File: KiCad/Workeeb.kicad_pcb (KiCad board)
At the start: 2 copper layers, 224 parts, among them J1 USB_C_Receptacle_USB2.0, U1 EFM32HG322F64G-C-QFP48

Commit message: Connect up row diodes
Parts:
- moved C_DEC1 118.9 mm to (468.0, 28.1)
- moved C_IOVDD_3 118.9 mm to (468.0, 31.1)
- moved C_VDD_1 118.9 mm to (465.8, 34.1)
- moved C_VREGI1 118.9 mm to (451.5, 23.6)
- moved C_AVDD1 118.9 mm to (463.6, 29.6)
- moved C_AVDD_0 118.9 mm to (463.6, 26.6)
- moved C_DEC2 118.9 mm to (474.7, 32.7)
- moved C_IOVDD1 118.9 mm to (460.4, 23.6)
- moved C_IOVDD_5 118.9 mm to (470.2, 37.1)
- moved C_RESET1 118.9 mm to (470.2, 34.1)
- moved C_VDD1 118.9 mm to (474.7, 35.7)
- moved C_VREGO1 118.9 mm to (456.0, 23.6)
- moved FB_VBUS1 118.9 mm to (465.6, 18.6)
- moved R_CC1 118.9 mm to (454.7, 29.5)
- moved R_CC2 118.9 mm to (454.7, 26.6)
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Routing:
- net ROW2: track 0.00 -> 380.6 mm
- net ROW6: track 0.00 -> 372.6 mm
- net ROW5: track 0.00 -> 354.6 mm
- net ROW4: track 0.00 -> 347.2 mm
- net ROW3: track 47.5 -> 352.1 mm
- net Net-(D100-Pad2): track 0.00 -> 22.0 mm
- net Net-(D69-Pad2): track 0.00 -> 19.0 mm
- net Net-(D7-Pad2): track 0.00 -> 19.0 mm
- net ROW1: track 295.2 -> 313.9 mm
- net Net-(D73-Pad2): track 0.00 -> 16.5 mm
- net Net-(D92-Pad2): track 0.00 -> 15.8 mm
- net Net-(D70-Pad2): track 0.00 -> 14.2 mm
- net Net-(D4-Pad2): track 0.00 -> 14.2 mm
- net Net-(D3-Pad2): track 0.00 -> 11.0 mm
- net Net-(D5-Pad2): track 0.00 -> 9.46 mm
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
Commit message: Route all left-side cols to MCU area
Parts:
- turned U1 to -90 degrees
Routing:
- net COL1: track 0.00 -> 457.3 mm, vias 0 -> 1
- net COL4: track 0.00 -> 409.2 mm, vias 0 -> 1
- net COL3: track 0.00 -> 403.0 mm, vias 0 -> 1
- net COL2: track 0.00 -> 387.6 mm, vias 0 -> 1
- net COL5: track 0.00 -> 367.7 mm, vias 0 -> 1
- net COL6: track 0.00 -> 347.2 mm, vias 0 -> 1
- net COL7: track 0.00 -> 333.9 mm, vias 0 -> 1
- net COL8: track 0.00 -> 317.1 mm, vias 0 -> 1
- net COL9: track 0.00 -> 297.3 mm, vias 0 -> 1
- net COL11: track 0.00 -> 291.7 mm, vias 0 -> 1
- net COL10: track 0.00 -> 278.9 mm, vias 0 -> 1
- net COL12: track 0.00 -> 252.8 mm, vias 0 -> 1
- net COL13: track 0.00 -> 233.6 mm, vias 0 -> 1
- net COL14: track 0.00 -> 227.2 mm, vias 0 -> 1
- net COL15: track 0.00 -> 199.2 mm, vias 0 -> 1
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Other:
- board text added: "25 mils for via placement"
- board text added: "31.25 mils for Diode placement"

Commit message: Reorder row/cols to match physical layout of routes better
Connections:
- U1 pad 11: COL2 -> ROW1
- U1 pad 12: COL3 -> ROW2
- U1 pad 13: COL4 -> ROW3
- U1 pad 14: unconnected-(U1-Pad14) -> ROW4
- U1 pad 15: unconnected-(U1-Pad15) -> ROW5
- U1 pad 17: unconnected-(U1-Pad17) -> ROW6
- U1 pad 2: ROW1 -> COL7
- U1 pad 25: COL5 -> BADGE
- U1 pad 26: COL6 -> NUMLK
- U1 pad 27: COL7 -> CAPS
- U1 pad 3: ROW2 -> COL6
- U1 pad 30: COL8 -> COL20
- U1 pad 31: COL9 -> COL19
- U1 pad 32: COL10 -> COL18
- U1 pad 37: COL11 -> COL17
- U1 pad 38: COL12 -> COL16
- U1 pad 39: COL13 -> COL15
- U1 pad 41: COL15 -> COL13
- U1 pad 42: COL16 -> COL12
- U1 pad 45: COL17 -> COL11
- U1 pad 46: COL18 -> COL10
- U1 pad 47: COL19 -> COL9
- U1 pad 48: COL20 -> COL8
- U1 pad 6: ROW3 -> COL5
- U1 pad 7: ROW4 -> COL4
- U1 pad 8: ROW5 -> COL3
- U1 pad 9: ROW6 -> COL2
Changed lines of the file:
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@@
   (net 131 "COL20")
   (net 132 "Net-(C_DEC1-Pad1)")
-  (net 133 "unconnected-(U1-Pad14)")
-  (net 134 "unconnected-(U1-Pad15)")
+  (net 133 "BADGE")
+  (net 134 "NUMLK")
   (net 135 "RESET")
-  (net 136 "unconnected-(U1-Pad17)")
+  (net 136 "CAPS")
   (net 137 "VBUS")
   (net 138 "Net-(FB_VBUS1-Pad1)")
@@
       (net 150 "DMPU") (pinfunction "PA0") (pintype "bidirectional"))
     (pad "2" smd rect locked (at -4.1148 2.250001 180) (size 0.254 1.461999) (layers "B.Cu" "B.Paste" "B.Mask")
-      (net 1 "ROW1") (pinfunction "PA1") (pintype "bidirectional"))
+      (net 19 "COL7") (pinfunction "PA1") (pintype "bidirectional"))
     (pad "3" smd rect locked (at -4.1148 1.749999 180) (size 0.254 1.461999) (layers "B.Cu" "B.Paste" "B.Mask")
-      (net 2 "ROW2") (pinfunction "PA2") (pintype "bidirectional"))
+      (net 17 "COL6") (pinfunction "PA2") (pintype "bidirectional"))
     (pad "4" smd rect locked (at -4.1148 1.25 180) (size 0.254 1.461999) (layers "B.Cu" "B.Paste" "B.Mask")
       (net 126 "VDD") (pinfunction "IOVDD_0") (pintype "power_in"))
@@
       (net 127 "GND") (pinfunction "VSS") (pintype "power_in"))
     (pad "6" smd rect locked (at -4.1148 0.25 180) (size 0.254 1.461999) (layers "B.Cu" "B.Paste" "B.Mask")
-      (net 4 "ROW3") (pinfunction "PC0") (pintype "bidirectional"))
+      (net 16 "COL5") (pinfunction "PC0") (pintype "bidirectional"))
     (pad "7" smd rect locked (at -4.1148 -0.25 180) (size 0.254 1.461999) (layers "B.Cu" "B.Paste" "B.Mask")
-      (net 6 "ROW4") (pinfunction "PC1") (pintype "bidirectional"))
+      (net 15 "COL4") (pinfunction "PC1") (pintype "bidirectional"))
     (pad "8" smd rect locked (at -4.1148 -0.750001 180) (size 0.254 1.461999) (layers "B.Cu" "B.Paste" "B.Mask")
-      (net 9 "ROW5") (pinfunction "PC2") (pintype "bidirectional"))
+      (net 13 "COL3") (pinfunction "PC2") (pintype "bidirectional"))
     (pad "9" smd rect locked (at -4.1148 -1.25 180) (size 0.254 1.461999) (layers "B.Cu" "B.Paste" "B.Mask")
-      (net 8 "ROW6") (pinfunction "PC3") (pintype "bidirectional"))
+      (net 12 "COL2") (pinfunction "PC3") (pintype "bidirectional"))
     (pad "10" smd rect locked (at -4.1148 -1.749999 180) (size 0.254 1.461999) (layers "B.Cu" "B.Paste" "B.Mask")
       (net 11 "COL1") (pinfunction "PC4") (pintype "bidirectional"))
     (pad "11" smd rect locked (at -4.1148 -2.250001 180) (size 0.254 1.461999) (layers "B.Cu" "B.Paste" "B.Mask")
-      (net 12 "COL2") (pinfunction "PB7") (pintype "bidirectional"))
+      (net 1 "ROW1") (pinfunction "PB7") (pintype "bidirectional"))
     (pad "12" smd rect locked (at -4.1148 -2.75 180) (size 0.254 1.461999) (layers "B.Cu" "B.Paste" "B.Mask")
-      (net 13 "COL3") (pinfunction "PB8") (pintype "bidirectional"))
+      (net 2 "ROW2") (pinfunction "PB8") (pintype "bidirectional"))
     (pad "13" smd rect locked (at -2.75 -4.1148 270) (size 0.254 1.461999) (layers "B.Cu" "B.Paste" "B.Mask")
-      (net 15 "COL4") (pinfunction "PA8") (pintype "bidirectional"))
+      (net 4 "ROW3") (pinfunction "PA8") (pintype "bidirectional"))
     (pad "14" smd rect locked (at -2.250001 -4.1148 270) (size 0.254 1.461999) (layers "B.Cu" "B.Paste" "B.Mask")
-      (net 133 "unconnected-(U1-Pad14)") (pinfunction "PA9") (pintype "bidirectional+no_connect"))
+      (net 6 "ROW4") (pinfunction "PA9") (pintype "bidirectional"))
     (pad "15" smd rect locked (at -1.749999 -4.1148 270) (size 0.254 1.461999) (layers "B.Cu" "B.Paste" "B.Mask")
-      (net 134 "unconnected-(U1-Pad15)") (pinfunction "PA10") (pintype "bidirectional+no_connect"))
+      (net 9 "ROW5") (pinfunction "PA10") (pintype "bidirectional"))
     (pad "16" smd rect locked (at -1.25 -4.1148 270) (size 0.254 1.461999) (layers "B.Cu" "B.Paste" "B.Mask")
       (net 135 "RESET") (pinfunction "RESETn") (pintype "unspecified"))
     (pad "17" smd rect locked (at -0.750001 -4.1148 270) (size 0.254 1.461999) (layers "B.Cu" "B.Paste" "B.Mask")
-      (net 136 "unconnected-(U1-Pad17)") (pinfunction "PB11") (pintype "bidirectional+no_connect"))
+      (net 8 "ROW6") (pinfunction "PB11") (pintype "bidirectional"))
     (pad "18" smd rect locked (at -0.25 -4.1148 270) (size 0.254 1.461999) (layers "B.Cu" "B.Paste" "B.Mask")
       (net 127 "GND") (pinfunction "VSS") (pintype "power_in"))
@@
       (net 143 "unconnected-(U1-Pad24)") (pinfunction "PD4") (pintype "bidirectional+no_connect"))
     (pad "25" smd rect locked (at 4.1148 -2.75 180) (size 0.254 1.461999) (layers "B.Cu" "B.Paste" "B.Mask")
-      (net 16 "COL5") (pinfunction "PD5") (pintype "bidirectional"))
+      (net 133 "BADGE") (pinfunction "PD5") (pintype "bidirectional"))
     (pad "26" smd rect locked (at 4.1148 -2.250001 180) (size 0.254 1.461999) (layers "B.Cu" "B.Paste" "B.Mask")
-      (net 17 "COL6") (pinfunction "PD6") (pintype "bidirectional"))
+      (net 134 "NUMLK") (pinfunction "PD6") (pintype "bidirectional"))
     (pad "27" smd rect locked (at 4.1148 -1.749999 180) (size 0.254 1.461999) (layers "B.Cu" "B.Paste" "B.Mask")
-      (net 19 "COL7") (pinfunction "PD7") (pintype "bidirectional"))
+      (net 136 "CAPS") (pinfunction "PD7") (pintype "bidirectional"))
     (pad "28" smd rect locked (at 4.1148 -1.25 180) (size 0.254 1.461999) (layers "B.Cu" "B.Paste" "B.Mask")
       (net 126 "VDD") (pinfunction "VDD_DREG") (pintype "power_in"))
@@
       (net 132 "Net-(C_DEC1-Pad1)") (pinfunction "DECOUPLE") (pintype "unspecified"))
     (pad "30" smd rect locked (at 4.1148 -0.25 180) (size 0.254 1.461999) (layers "B.Cu" "B.Paste" "B.Mask")
-      (net 20 "COL8") (pinfunction "PC8") (pintype "bidirectional"))
+      (net 131 "COL20") (pinfunction "PC8") (pintype "bidirectional"))
     (pad "31" smd rect locked (at 4.1148 0.25 180) (size 0.254 1.461999) (layers "B.Cu" "B.Paste" "B.Mask")
-      (net 21 "COL9") (pinfunction "PC9") (pintype "bidirectional"))
+      (net 130 "COL19") (pinfunction "PC9") (pintype "bidirectional"))
     (pad "32" smd rect locked (at 4.1148 0.750001 180) (size 0.254 1.461999) (layers "B.Cu" "B.Paste" "B.Mask")
-      (net 26 "COL10") (pinfunction "PC10") (pintype "bidirectional"))
+      (net 129 "COL18") (pinfunction "PC10") (pintype "bidirectional"))
     (pad "33" smd rect locked (at 4.1148 1.25 180) (size 0.254 1.461999) (layers "B.Cu" "B.Paste" "B.Mask")
       (net 137 "VBUS") (pinfunction "USB_VREGI") (pintype "unspecified"))
@@
       (net 148 "D+") (pinfunction "PC15") (pintype "bidirectional"))
     (pad "37" smd rect locked (at 2.75 4.1148 270) (size 0.254 1.461999) (layers "B.Cu" "B.Paste" "B.Mask")
-      (net 29 "COL11") (pinfunction "PF0") (pintype "bidirectional"))
+      (net 128 "COL17") (pinfunction "PF0") (pintype "bidirectional"))
     (pad "38" smd rect locked (at 2.250001 4.1148 270) (size 0.254 1.461999) (layers "B.Cu" "B.Paste" "B.Mask")
-      (net 33 "COL12") (pinfunction "PF1") (pintype "bidirectional"))
+      (net 125 "COL16") (pinfunction "PF1") (pintype "bidirectional"))
     (pad "39" smd rect locked (at 1.749999 4.1148 270) (size 0.254 1.461999) (layers "B.Cu" "B.Paste" "B.Mask")
-      (net 37 "COL13") (pinfunction "PF2") (pintype "bidirectional"))
+      (net 124 "COL15") (pinfunction "PF2") (pintype "bidirectional"))
     (pad "40" smd rect locked (at 1.25 4.1148 270) (size 0.254 1.461999) (layers "B.Cu" "B.Paste" "B.Mask")
       (net 123 "COL14") (pinfunction "PF3") (pintype "bidirectional"))
     (pad "41" smd rect locked (at 0.750001 4.1148 270) (size 0.254 1.461999) (layers "B.Cu" "B.Paste" "B.Mask")
-      (net 124 "COL15") (pinfunction "PF4") (pintype "bidirectional"))
+      (net 37 "COL13") (pinfunction "PF4") (pintype "bidirectional"))
     (pad "42" smd rect locked (at 0.25 4.1148 270) (size 0.254 1.461999) (layers "B.Cu" "B.Paste" "B.Mask")
-      (net 125 "COL16") (pinfunction "PF5") (pintype "bidirectional"))
+      (net 33 "COL12") (pinfunction "PF5") (pintype "bidirectional"))
     (pad "43" smd rect locked (at -0.25 4.1148 270) (size 0.254 1.461999) (layers "B.Cu" "B.Paste" "B.Mask")
       (net 126 "VDD") (pinfunction "IOVDD_5") (pintype "power_in"))
@@
       (net 127 "GND") (pinfunction "VSS") (pintype "power_in"))
     (pad "45" smd rect locked (at -1.25 4.1148 270) (size 0.254 1.461999) (layers "B.Cu" "B.Paste" "B.Mask")
-      (net 128 "COL17") (pinfunction "PE10") (pintype "bidirectional"))
+      (net 29 "COL11") (pinfunction "PE10") (pintype "bidirectional"))
     (pad "46" smd rect locked (at -1.749999 4.1148 270) (size 0.254 1.461999) (layers "B.Cu" "B.Paste" "B.Mask")
-      (net 129 "COL18") (pinfunction "PE11") (pintype "bidirectional"))
+      (net 26 "COL10") (pinfunction "PE11") (pintype "bidirectional"))
     (pad "47" smd rect locked (at -2.250001 4.1148 270) (size 0.254 1.461999) (layers "B.Cu" "B.Paste" "B.Mask")
-      (net 130 "COL19") (pinfunction "PE12") (pintype "bidirectional"))
+      (net 21 "COL9") (pinfunction "PE12") (pintype "bidirectional"))
     (pad "48" smd rect locked (at -2.75 4.1148 270) (size 0.254 1.461999) (layers "B.Cu" "B.Paste" "B.Mask")
-      (net 131 "COL20") (pinfunction "PE13") (pintype "bidirectional"))
+      (net 20 "COL8") (pinfunction "PE13") (pintype "bidirectional"))
   )
   (footprint "Diode_SMD:D_SOD-123" (layer "B.Cu")

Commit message: Moved diodes into new place for better col routing
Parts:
- moved D100 16.2 mm to (426.2, 94.5)
- moved D97 10.7 mm to (406.4, 142.1), turned to 90 degrees
- moved D95 10.7 mm to (406.4, 104.0), turned to 90 degrees
- moved D19 10.7 mm to (97.6, 142.1), turned to 90 degrees
- moved D34 10.7 mm to (167.5, 142.1), turned to 90 degrees
- moved D5 10.7 mm to (50.0, 142.1), turned to 90 degrees
- moved D55 10.7 mm to (235.7, 142.1), turned to 90 degrees
- moved D61 10.7 mm to (254.8, 142.1), turned to 90 degrees
- moved D66 10.7 mm to (273.8, 142.1), turned to 90 degrees
- moved D8 10.7 mm to (73.8, 142.1), turned to 90 degrees
- moved D92 10.7 mm to (388.1, 142.1), turned to 90 degrees
- moved D11 10.7 mm to (73.8, 84.9), turned to 90 degrees
- moved D16 10.7 mm to (92.9, 84.9), turned to 90 degrees
- moved D22 10.7 mm to (111.9, 84.9), turned to 90 degrees
- moved D27 10.7 mm to (131.0, 84.9), turned to 90 degrees
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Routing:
- net ROW3: track 352.1 -> 396.0 mm
- net ROW5: track 354.6 -> 391.2 mm
- net ROW6: track 372.6 -> 360.3 mm
- net Net-(D100-Pad2): track 22.0 -> 10.3 mm
- net Net-(D12-Pad2): track 6.29 -> 10.3 mm
- net Net-(D89-Pad2): track 6.29 -> 10.3 mm
- net Net-(D85-Pad2): track 6.29 -> 10.3 mm
- net Net-(D79-Pad2): track 6.29 -> 10.3 mm
- net Net-(D39-Pad2): track 6.29 -> 10.3 mm
- net Net-(D29-Pad2): track 6.29 -> 10.3 mm
- net Net-(D3-Pad2): track 11.0 -> 14.8 mm
- net Net-(D92-Pad2): track 15.8 -> 19.6 mm
- net Net-(D93-Pad2): track 6.93 -> 10.3 mm
- net Net-(D88-Pad2): track 6.93 -> 10.3 mm
- net Net-(D78-Pad2): track 6.93 -> 10.3 mm
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
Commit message: Removed old vias
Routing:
- net COL15: track 199.2 -> 213.4 mm, vias 1 -> 0
- net COL17: track 84.2 -> 93.7 mm, vias 1 -> 0
- net COL9: track 297.3 -> 291.8 mm, vias 1 -> 0
- net COL11: track 291.7 -> 286.3 mm, vias 1 -> 0
- net COL10: track 278.9 -> 273.5 mm, vias 1 -> 0
- net COL8: track 317.1 -> 311.7 mm, vias 1 -> 0
- net COL7: track 333.9 -> 329.5 mm, vias 1 -> 0
- net COL2: track 387.6 -> 383.2 mm, vias 1 -> 0
- net COL13: track 233.6 -> 237.7 mm, vias 1 -> 0
- net COL12: track 252.8 -> 257.0 mm, vias 1 -> 0
- net COL3: track 403.0 -> 406.7 mm, vias 1 -> 0
- net COL1: track 457.3 -> 460.4 mm, vias 1 -> 0
- net COL6: track 347.2 -> 350.2 mm, vias 1 -> 0
- net COL5: track 367.7 -> 370.8 mm, vias 1 -> 0
- net COL16: track 151.8 -> 154.8 mm, vias 1 -> 0
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
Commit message: Start to do power routing
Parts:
- removed C_AVDD_0: 10nF, Capacitor_SMD:C_0805_2012Metric
- removed C_IOVDD_0, C_IOVDD_5: 0.1uF, Capacitor_SMD:C_0805_2012Metric
- added C_AVDD_2: 10nF, Capacitor_SMD:C_0805_2012Metric, F.Cu at (468.8, -5.03)
- added C_IOVDD_1: 0.1uF, Capacitor_SMD:C_0805_2012Metric, F.Cu at (466.8, -8.04)
- added C_IOVDD_2: 0.1uF, Capacitor_SMD:C_0805_2012Metric, F.Cu at (453.2, -3.17)
- added D101: SK6812, LED_SMD:LED_SK6812_PLCC4_5.0x5.0mm_P3.2mm, F.Cu at (416.7, 33.3)
- added D102: LED, LED_SMD:LED_1206_3216Metric_Pad1.42x1.75mm_HandSolder, F.Cu at (378.6, 33.3)
- added D103: LED, LED_SMD:LED_1206_3216Metric_Pad1.42x1.75mm_HandSolder, F.Cu at (397.7, 33.3)
- MX83: value Knob -> Num Lock; footprint Rotary_Encoder:RotaryEncoder_Alps_EC12E-Switch_Vertical_H20mm -> MX_Only:MXOnly-1U-NoLED
- MX84: value Num Lock -> num7
- MX85: value num7 -> num4
- MX86: value num4 -> num1
- MX87: value num1 -> Knob; footprint MX_Only:MXOnly-1U-NoLED -> Rotary_Encoder:RotaryEncoder_Alps_EC12E-Switch_Vertical_H20mm
- moved MX87 93.0 mm to (362.1, 26.1), turned to -90 degrees
- moved MX83 35.8 mm to (359.6, 61.9), turned to 0 degrees
- moved MX84 19.1 mm to (359.6, 81.0)
- moved MX85 19.0 mm to (359.6, 100.0)
- moved MX86 19.0 mm to (359.6, 119.1)
- moved C_VREGI1 13.2 mm to (442.1, 14.3)
- moved U1 4.48 mm to (386.6, 45.2)
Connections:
- MX84 pad 2: Net-(D84-Pad2) -> Net-(D85-Pad2)
- MX85 pad 2: Net-(D85-Pad2) -> Net-(D86-Pad2)
- MX86 pad 2: Net-(D86-Pad2) -> Net-(D87-Pad2)
- R_CC1 pad 1: Net-(J1-PadA5) -> Net-(J1-PadB5)
- R_CC2 pad 1: Net-(J1-PadB5) -> Net-(J1-PadA5)
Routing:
- net VDD: track 0.00 -> 11.5 mm, vias 0 -> 6

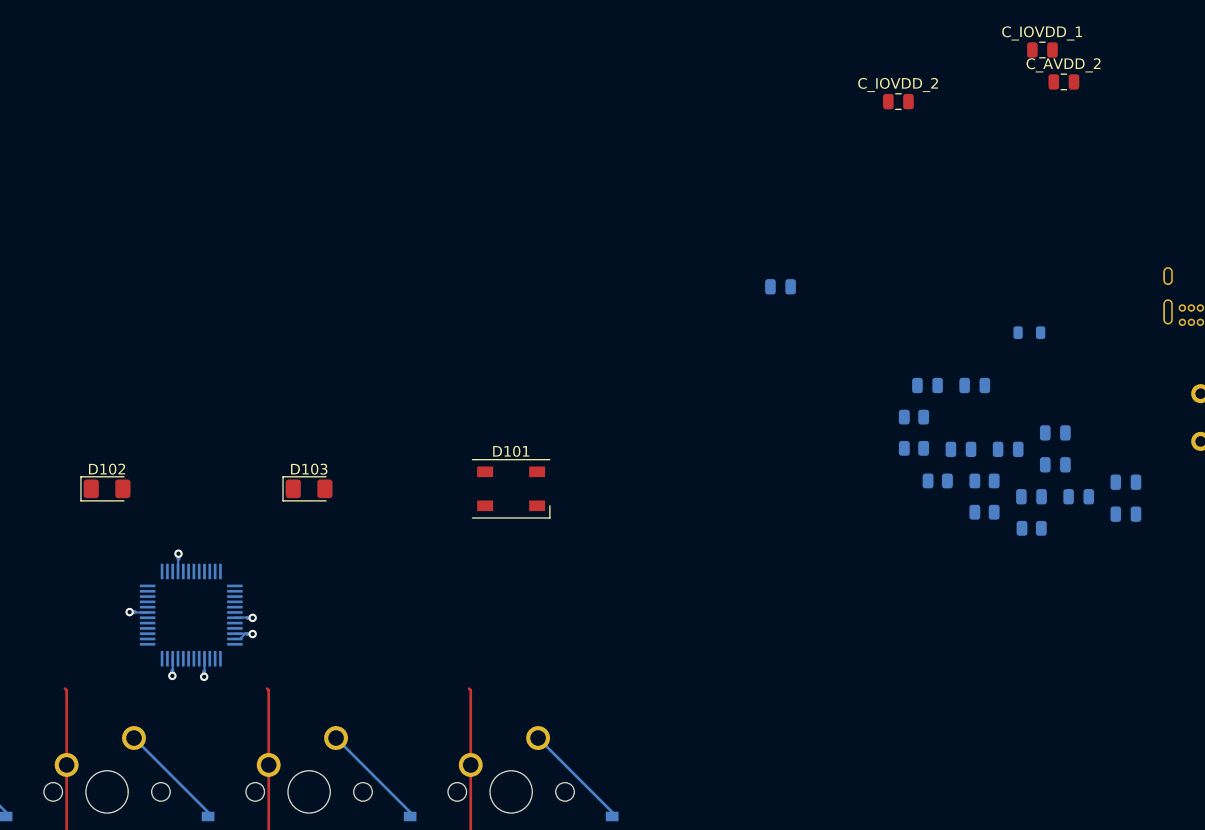
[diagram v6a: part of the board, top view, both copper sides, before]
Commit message: Better cap names, start placing decoupling caps
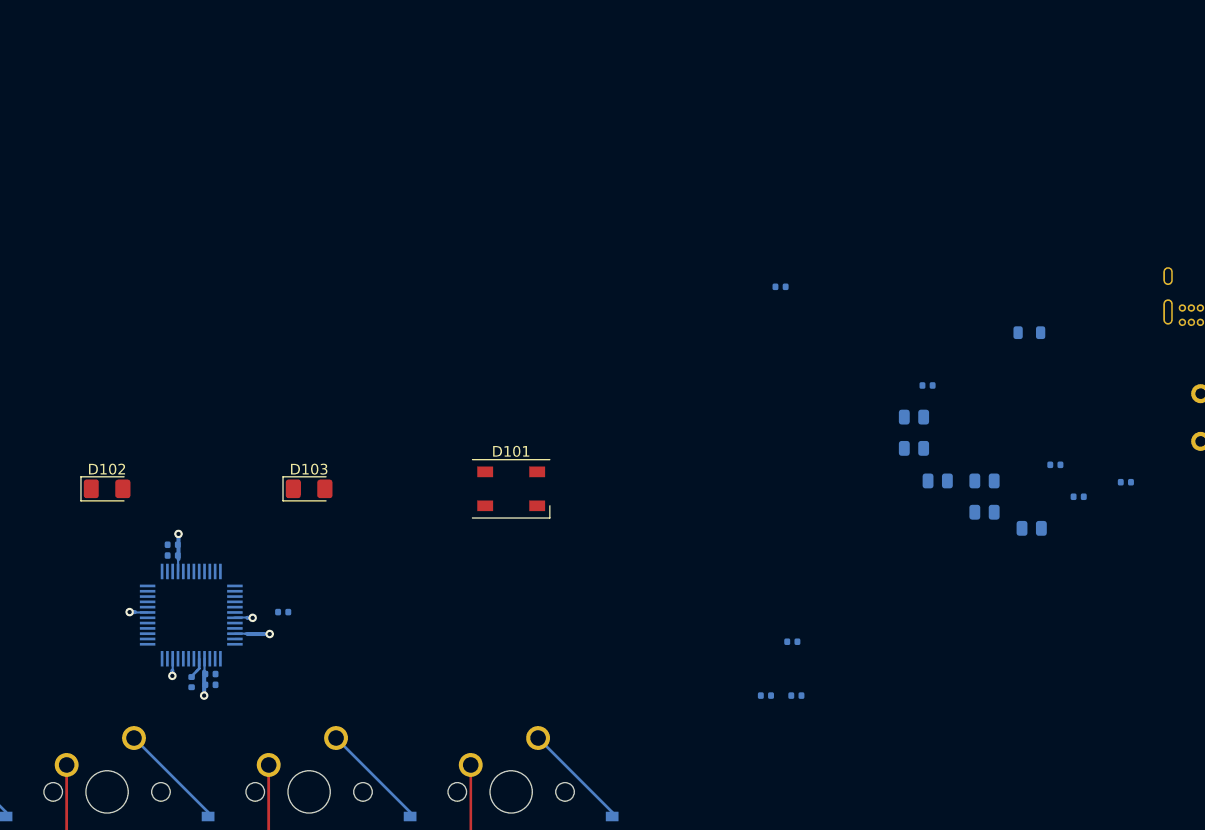
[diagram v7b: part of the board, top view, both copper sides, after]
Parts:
- removed C_AVDD1, C_IOVDD1, C_VDD1: 10uF, Capacitor_SMD:C_0805_2012Metric
- removed C_AVDD_2: 10nF, Capacitor_SMD:C_0805_2012Metric
- removed C_IOVDD_1, C_IOVDD_2, C_VDD_1: 0.1uF, Capacitor_SMD:C_0805_2012Metric
- added C_AVDD0: 10uF, Capacitor_SMD:C_0402_1005Metric, B.Cu at (440.7, 52.8)
- added C_AVDD_0: 10nF, Capacitor_SMD:C_0402_1005Metric, B.Cu at (443.6, 52.8)
- added C_DREG1: 0.1uF, Capacitor_SMD:C_0402_1005Metric, B.Cu at (388.4, 50.8)
- added C_DREG2: 10uF, Capacitor_SMD:C_0402_1005Metric, B.Cu at (388.4, 51.8)
- added C_IOVDD0: 10uF, Capacitor_SMD:C_0402_1005Metric, B.Cu at (384.8, 38.6)
- added C_IOVDD_0: 0.1uF, Capacitor_SMD:C_0402_1005Metric, B.Cu at (384.8, 39.6)
- added C_IOVDD_5: 0.1uF, Capacitor_SMD:C_0402_1005Metric, B.Cu at (443.2, 47.8)
- C_AVDD_1, C_DEC1, C_DEC2, C_IOVDD_3, C_RESET1, C_VREGI1, C_VREGO1: footprint Capacitor_SMD:C_0805_2012Metric -> Capacitor_SMD:C_0402_1005Metric
- moved C_DEC1 84.8 mm to (386.6, 51.6), turned to -90 degrees
- moved C_AVDD_1 65.7 mm to (395.2, 45.0)
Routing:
- net COL20: track 73.6 -> 66.3 mm
- net COL19: track 83.1 -> 75.8 mm
- net COL18: track 87.3 -> 80.0 mm
- net VDD: track 11.5 -> 16.0 mm
- net Net-(C_DEC1-Pad1): track 0.00 -> 1.99 mm
